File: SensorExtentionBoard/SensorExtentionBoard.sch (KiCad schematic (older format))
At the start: 0 parts

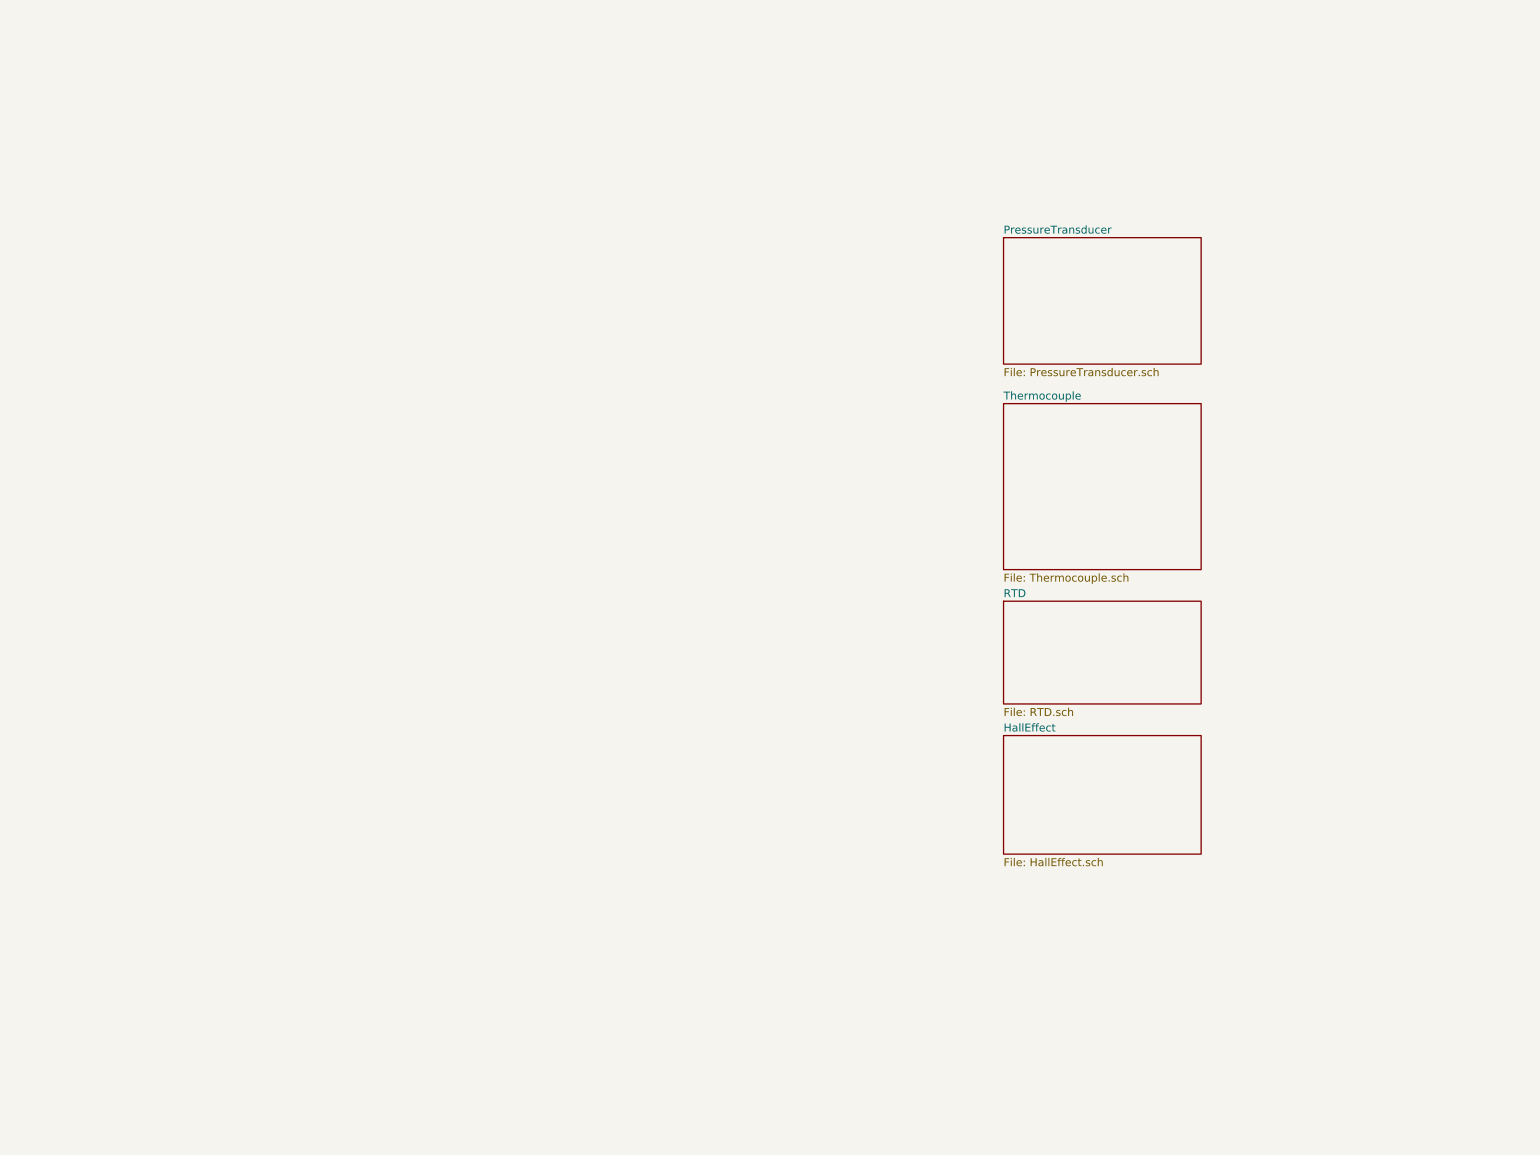
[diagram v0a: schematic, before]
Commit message: Added top level page and made various fixes in other pages of SEB test rig board
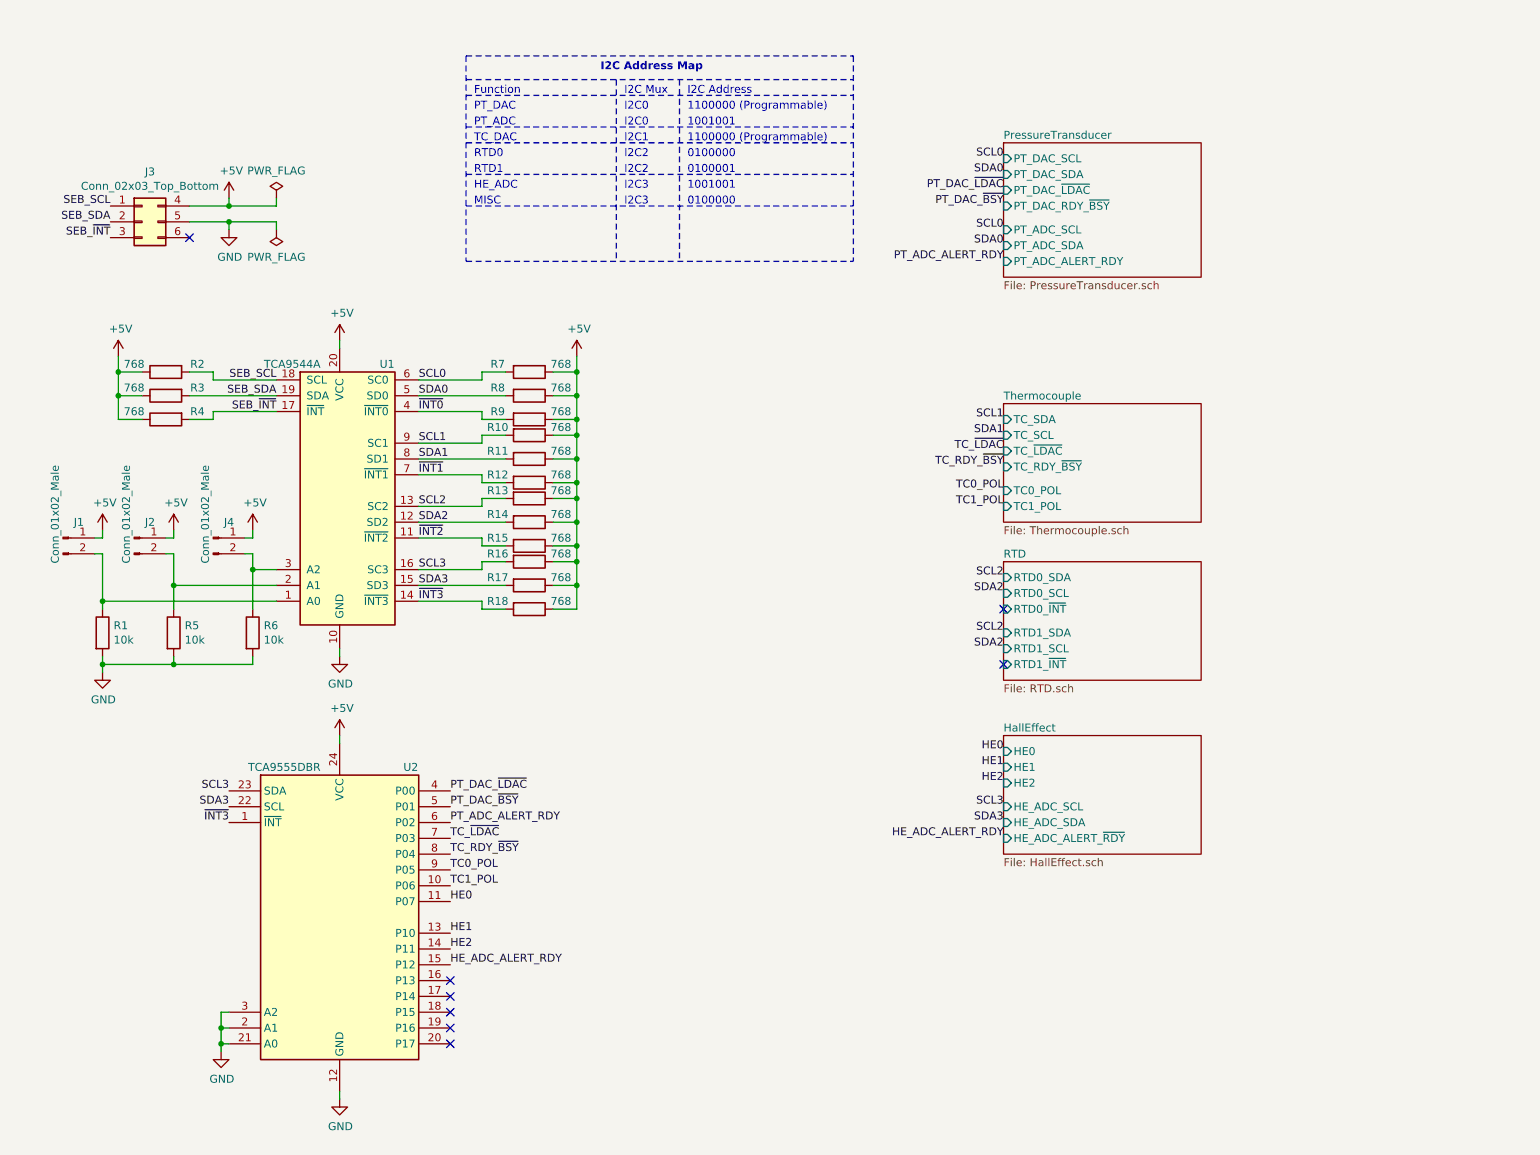
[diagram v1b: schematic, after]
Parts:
- added J1, J2, J4: Conn_01x02_Male, symbol Connector:Conn_01x02_Male
- added J3: Conn_02x03_Top_Bottom, symbol Connector_Generic:Conn_02x03_Top_Bottom
- added R1, R5, R6: 10k, Resistor_SMD:R_1206_3216Metric_Pad1.42x1.75mm_HandSolder, symbol Device:R
- added R10, R11, R12, R13, R14, R15, R16, R17, R18, R2, R3, R4, R7, R8, R9: 768, Resistor_SMD:R_1206_3216Metric_Pad1.42x1.75mm_HandSolder, symbol Device:R
- added U1: TCA9544A, Package_SO:TSSOP-20_4.4x6.5mm_P0.65mm, symbol Interface_Expansion:TCA9544A
- added U2: TCA9555DBR, Package_SO:SSOP-24_5.3x8.2mm_P0.65mm, symbol Interface_Expansion:TCA9555DBR
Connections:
- new net: J4.2 (Pin_2), R6.1, U1.3 (A2)
- new net: J2.2 (Pin_2), R5.1, U1.2 (A1)
- new net: J1.2 (Pin_2), R1.1, U1.1 (A0)
- new net +5V: J1.1 (Pin_1), J2.1 (Pin_1), J3.4 (Pin_4), J4.1 (Pin_1), R10.1, R11.1, R12.1, R13.1, R14.1, R15.1, R16.1, R17.1, R18.1, R2.1, R3.1, R4.1, R7.1, R8.1, R9.1, U1.20 (VCC), U2.24 (VCC)
- new net GND: J3.5 (Pin_5), R1.2, R5.2, R6.2, U1.10 (GND), U2.12 (GND), U2.2 (A1), U2.21 (A0), U2.3 (A2)
- new net HE0: U2.11 (P07)
- new net HE1: U2.13 (P10)
- new net HE2: U2.14 (P11)
- new net HE_ADC_ALERT_RDY: U2.15 (P12)
- new net PT_ADC_ALERT_RDY: U2.6 (P02)
- new net PT_DAC_~BSY: U2.5 (P01)
- new net PT_DAC_~LDAC: U2.4 (P00)
- new net SCL0: R7.2, U1.6 (SC0)
- new net SCL1: R10.2, U1.9 (SC1)
- new net SCL2: R13.2, U1.13 (SC2)
- new net SCL3: R16.2, U1.16 (SC3), U2.23 (SDA)
- new net SDA0: R8.2, U1.5 (SD0)
- new net SDA1: R11.2, U1.8 (SD1)
- new net SDA2: R14.2, U1.12 (SD2)
- new net SDA3: R17.2, U1.15 (SD3), U2.22 (SCL)
- new net SEB_SCL: J3.1 (Pin_1), R2.2, U1.18 (SCL)
- new net SEB_SDA: J3.2 (Pin_2), R3.2, U1.19 (SDA)
- new net SEB_~INT: J3.3 (Pin_3), R4.2, U1.17 (~INT)
- new net TC0_POL: U2.9 (P05)
- new net TC1_POL: U2.10 (P06)
- new net TC_RDY_~BSY: U2.8 (P04)
- new net TC_~LDAC: U2.7 (P03)
- new net ~INT0: R9.2, U1.4 (~INT0)
- new net ~INT1: R12.2, U1.7 (~INT1)
- new net ~INT2: R15.2, U1.11 (~INT2)
- new net ~INT3: R18.2, U1.14 (~INT3), U2.1 (~INT)
- no-connect marks 0 -> 8
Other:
- note added: "0100000"
- note added: "0100001"
- note added: "1001001"
- note added: "1100000 (Programmable)"
- note added: "Function"
- note added: "HE_ADC"
- note added: "I2C Address"
- note added: "I2C Address Map"
- note added: "I2C Mux"
- note added: "I2C0"
- note added: "I2C1"
- note added: "I2C2"
- note added: "I2C3"
- note added: "MISC"
- note added: "PT_ADC"
- note added: "PT_DAC"
- note added: "RTD0"
- note added: "RTD1"
- note added: "TC_DAC"

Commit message: Moved some stuff and added footprints to components
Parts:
- J1, J2, J4: footprint (none) -> Connector_PinHeader_2.54mm:PinHeader_1x02_P2.54mm_Vertical
- J3: footprint (none) -> Connector_Molex:Molex_Micro-Fit_3.0_43045-0612_2x03_P3.00mm_Vertical
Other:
- note added: "I2C Address 1110xxx"
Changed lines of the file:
@@
 $EndDescr
 $Sheet
-S 6750 5050 1250 750
+S 8750 5100 1250 750
 U 5E059E7A
 F0 "HallEffect" 50
 F1 "HallEffect.sch" 50
-F2 "HE0" I L 6750 5150 50
-F3 "HE1" I L 6750 5250 50
-F4 "HE2" I L 6750 5350 50
-F5 "HE_ADC_ALERT_~RDY" I L 6750 5700 50
-F6 "HE_ADC_SCL" I L 6750 5500 50
-F7 "HE_ADC_SDA" I L 6750 5600 50
+F2 "HE0" I L 8750 5200 50
+F3 "HE1" I L 8750 5300 50
+F4 "HE2" I L 8750 5400 50
+F5 "HE_ADC_ALERT_~RDY" I L 8750 5750 50
+F6 "HE_ADC_SCL" I L 8750 5550 50
+F7 "HE_ADC_SDA" I L 8750 5650 50
 $EndSheet
 $Sheet
-S 6750 2950 1250 750
+S 8750 3000 1250 750
 U 5E059E8F
 F0 "Thermocouple" 50
 F1 "Thermocouple.sch" 50
-F2 "TC_SDA" I L 6750 3050 50
-F3 "TC_SCL" I L 6750 3150 50
-F4 "TC_~LDAC" I L 6750 3250 50
-F5 "TC_RDY_~BSY" I L 6750 3350 50
-F6 "TC0_POL" I L 6750 3500 50
-F7 "TC1_POL" I L 6750 3600 50
+F2 "TC_SDA" I L 8750 3100 50
+F3 "TC_SCL" I L 8750 3200 50
+F4 "TC_~LDAC" I L 8750 3300 50
+F5 "TC_RDY_~BSY" I L 8750 3400 50
+F6 "TC0_POL" I L 8750 3550 50
+F7 "TC1_POL" I L 8750 3650 50
 $EndSheet
 $Sheet
-S 6750 3950 1250 750
+S 8750 4000 1250 750
 U 5E059E9F
 F0 "RTD" 50
 F1 "RTD.sch" 50
-F2 "RTD0_SDA" I L 6750 4050 50
-F3 "RTD0_SCL" I L 6750 4150 50
-F4 "RTD0_~INT" I L 6750 4250 50
-F5 "RTD1_SDA" I L 6750 4400 50
-F6 "RTD1_SCL" I L 6750 4500 50
-F7 "RTD1_~INT" I L 6750 4600 50
+F2 "RTD0_SDA" I L 8750 4100 50
+F3 "RTD0_SCL" I L 8750 4200 50
+F4 "RTD0_~INT" I L 8750 4300 50
+F5 "RTD1_SDA" I L 8750 4450 50
+F6 "RTD1_SCL" I L 8750 4550 50
+F7 "RTD1_~INT" I L 8750 4650 50
 $EndSheet
 Text Label 2150 2800 2    50   ~ 0
@@
 F 0 "J3" H 1350 2117 50  0000 C CNN
 F 1 "Conn_02x03_Top_Bottom" H 1350 2026 50  0000 C CNN
-F 2 "" H 1300 1800 50  0001 C CNN
+F 2 "Connector_Molex:Molex_Micro-Fit_3.0_43045-0612_2x03_P3.00mm_Vertical" H 1300 1800 50  0001 C CNN
 F 3 "~" H 1300 1800 50  0001 C CNN
 	1    1300 1800
@@
 Connection ~ 1850 1700
 NoConn ~ 1600 1900
-Text Notes 3400 1000 0    50   ~ 0
+Text Notes 4800 1000 0    50   ~ 0
 Function
-Text Notes 4350 1000 0    50   ~ 0
+Text Notes 5750 1000 0    50   ~ 0
 I2C Mux
-Text Notes 4750 1000 0    50   ~ 0
+Text Notes 6150 1000 0    50   ~ 0
 I2C Address
 Wire Notes Line style solid
-	4300 900  4300 2050
+	5700 900  5700 2050
 Wire Notes Line style solid
-	4700 900  4700 2050
-Text Notes 4200 850  0    50   ~ 10
+	6100 900  6100 2050
+Text Notes 5600 850  0    50   ~ 10
 I2C Address Map
 Wire Notes Line style solid
-	3350 750  3350 2050
+	4750 750  4750 2050
 Wire Notes Line style solid
-	5800 750  5800 2050
-Text Notes 4750 1100 0    50   ~ 0
+	7200 750  7200 2050
+Text Notes 6150 1100 0    50   ~ 0
 1100000 (Programmable)
-Text Notes 3400 1100 0    50   ~ 0
+Text Notes 4800 1100 0    50   ~ 0
 PT_DAC
-Text Notes 4350 1100 0    50   ~ 0
+Text Notes 5750 1100 0    50   ~ 0
 I2C0
 Wire Notes Line style solid
-	3350 900  5800 900
+	4750 900  7200 900
 Wire Notes Line style solid
-	3350 750  5800 750
+	4750 750  7200 750
 Wire Notes Line style solid
-	3350 2050 5800 2050
-Text Notes 3400 1200 0    50   ~ 0
+	4750 2050 7200 2050
+Text Notes 4800 1200 0    50   ~ 0
 PT_ADC
-Text Notes 4750 1200 0    50   ~ 0
+Text Notes 6150 1200 0    50   ~ 0
 1001001
-Text Notes 4350 1200 0    50   ~ 0
+Text Notes 5750 1200 0    50   ~ 0
 I2C0
-Text Notes 4750 1300 0    50   ~ 0
+Text Notes 6150 1300 0    50   ~ 0
 1100000 (Programmable)
-Text Notes 4350 1300 0    50   ~ 0
+Text Notes 5750 1300 0    50   ~ 0
 I2C1
-Text Notes 3400 1300 0    50   ~ 0
+Text Notes 4800 1300 0    50   ~ 0
 TC_DAC
-Text Notes 3400 1400 0    50   ~ 0
+Text Notes 4800 1400 0    50   ~ 0
 RTD0
-Text Notes 3400 1500 0    50   ~ 0
+Text Notes 4800 1500 0    50   ~ 0
 RTD1
-Text Notes 4750 1400 0    50   ~ 0
+Text Notes 6150 1400 0    50   ~ 0
 0100000
-Text Notes 4750 1500 0    50   ~ 0
+Text Notes 6150 1500 0    50   ~ 0
 0100001
-Text Notes 4350 1400 0    50   ~ 0
+Text Notes 5750 1400 0    50   ~ 0
 I2C2
-Text Notes 4350 1500 0    50   ~ 0
+Text Notes 5750 1500 0    50   ~ 0
 I2C2
 Wire Notes Line style solid
-	3350 1000 5800 1000
+	4750 1000 7200 1000
 $Comp
 L power:GND #PWR02
@@
 F 0 "J4" H 1850 3900 50  0000 C CNN
 F 1 "Conn_01x02_Male" V 1700 3950 50  0000 C CNN
-F 2 "" H 1750 3800 50  0001 C CNN
+F 2 "Connector_PinHeader_2.54mm:PinHeader_1x02_P2.54mm_Vertical" H 1750 3800 50  0001 C CNN
 F 3 "~" H 1750 3800 50  0001 C CNN
 	1    1750 3800
@@
 F 0 "J2" H 1350 3900 50  0000 C CNN
 F 1 "Conn_01x02_Male" V 1200 3950 50  0000 C CNN
-F 2 "" H 1250 3800 50  0001 C CNN
+F 2 "Connector_PinHeader_2.54mm:PinHeader_1x02_P2.54mm_Vertical" H 1250 3800 50  0001 C CNN
 F 3 "~" H 1250 3800 50  0001 C CNN
 	1    1250 3800
@@
 F 0 "J1" H 900 3900 50  0000 C CNN
 F 1 "Conn_01x02_Male" V 750 3950 50  0000 C CNN
-F 2 "" H 800 3800 50  0001 C CNN
+F 2 "Connector_PinHeader_2.54mm:PinHeader_1x02_P2.54mm_Vertical" H 800 3800 50  0001 C CNN
 F 3 "~" H 800 3800 50  0001 C CNN
 	1    800  3800
@@
 Text Label 1100 1900 2    50   ~ 0
 SEB_~INT
-Text Notes 3400 1600 0    50   ~ 0
+Text Notes 4800 1600 0    50   ~ 0
 HE_ADC
-Text Notes 4350 1600 0    50   ~ 0
+Text Notes 5750 1600 0    50   ~ 0
 I2C3
-Text Notes 4750 1600 0    50   ~ 0
+Text Notes 6150 1600 0    50   ~ 0
 1001001
 Text Label 3050 2800 0    50   ~ 0
@@
 Text Label 3050 4200 0    50   ~ 0
 ~INT3
-Text Label 6750 1400 2    50   ~ 0
+Text Label 8750 2000 2    50   ~ 0
 SCL0
-Text Label 6750 1500 2    50   ~ 0
+Text Label 8750 2100 2    50   ~ 0
 SDA0
-Text Label 6750 1850 2    50   ~ 0
+Text Label 8750 2450 2    50   ~ 0
 SCL0
-Text Label 6750 1950 2    50   ~ 0
+Text Label 8750 2550 2    50   ~ 0
 SDA0
-Text Label 6750 3050 2    50   ~ 0
+Text Label 8750 3100 2    50   ~ 0
 SCL1
-Text Label 6750 3150 2    50   ~ 0
+Text Label 8750 3200 2    50   ~ 0
 SDA1
-Text Label 6750 4050 2    50   ~ 0
+Text Label 8750 4100 2    50   ~ 0
 SCL2
-Text Label 6750 4150 2    50   ~ 0
+Text Label 8750 4200 2    50   ~ 0
 SDA2
-Text Label 6750 4400 2    50   ~ 0
+Text Label 8750 4450 2    50   ~ 0
 SCL2
-Text Label 6750 4500 2    50   ~ 0
+Text Label 8750 4550 2    50   ~ 0
 SDA2
-Text Label 6750 5500 2    50   ~ 0
+Text Label 8750 5550 2    50   ~ 0
 SCL3
-Text Label 6750 5600 2    50   ~ 0
+Text Label 8750 5650 2    50   ~ 0
 SDA3
 $Comp
@@
 Wire Wire Line
 	2550 5050 2550 5100
-Text Notes 3400 1700 0    50   ~ 0
+Text Notes 4800 1700 0    50   ~ 0
 MISC
-Text Notes 4350 1700 0    50   ~ 0
+Text Notes 5750 1700 0    50   ~ 0
 I2C3
-Text Notes 4750 1700 0    50   ~ 0
+Text Notes 6150 1700 0    50   ~ 0
 0100000
 Wire Notes Line
-	3350 1200 5800 1200
+	4750 1200 7200 1200
 Wire Notes Line
-	3350 1300 5800 1300
+	4750 1300 7200 1300
 Wire Notes Line
-	3350 1500 5800 1500
+	4750 1500 7200 1500
 Wire Notes Line
-	3350 1700 5800 1700
+	4750 1700 7200 1700
 $Sheet
-S 6750 1300 1250 850
+S 8750 1900 1250 850
 U 5E059EAC
 F0 "PressureTransducer" 50
 F1 "PressureTransducer.sch" 50
-F2 "PT_DAC_SCL" I L 6750 1400 50
-F3 "PT_DAC_SDA" I L 6750 1500 50
-F4 "PT_DAC_RDY_~BSY" I L 6750 1700 50
-F5 "PT_ADC_SCL" I L 6750 1850 50
-F6 "PT_ADC_SDA" I L 6750 1950 50
-F7 "PT_ADC_ALERT_RDY" I L 6750 2050 50
-F8 "PT_DAC_~LDAC" I L 6750 1600 50
+F2 "PT_DAC_SCL" I L 8750 2000 50
+F3 "PT_DAC_SDA" I L 8750 2100 50
+F4 "PT_DAC_RDY_~BSY" I L 8750 2300 50
+F5 "PT_ADC_SCL" I L 8750 2450 50
+F6 "PT_ADC_SDA" I L 8750 2550 50
+F7 "PT_ADC_ALERT_RDY" I L 8750 2650 50
+F8 "PT_DAC_~LDAC" I L 8750 2200 50
 $EndSheet
 Text Label 3250 6100 0    50   ~ 0
@@
 Text Label 3250 6400 0    50   ~ 0
 HE2
-Text Label 6750 5350 2    50   ~ 0
+Text Label 8750 5400 2    50   ~ 0
 HE2
-Text Label 6750 5250 2    50   ~ 0
+Text Label 8750 5300 2    50   ~ 0
 HE1
-Text Label 6750 5150 2    50   ~ 0
+Text Label 8750 5200 2    50   ~ 0
 HE0
-Text Label 6750 3500 2    50   ~ 0
+Text Label 8750 3550 2    50   ~ 0
 TC0_POL
-Text Label 6750 3600 2    50   ~ 0
+Text Label 8750 3650 2    50   ~ 0
 TC1_POL
 Text Label 3250 5900 0    50   ~ 0
@@
 Text Label 3250 6000 0    50   ~ 0
 TC1_POL
-Text Label 6750 3250 2    50   ~ 0
+Text Label 8750 3300 2    50   ~ 0
 TC_~LDAC
-Text Label 6750 3350 2    50   ~ 0
+Text Label 8750 3400 2    50   ~ 0
 TC_RDY_~BSY
 Text Label 3250 5700 0    50   ~ 0
@@
 Text Label 3250 5800 0    50   ~ 0
 TC_RDY_~BSY
-Text Label 6750 1600 2    50   ~ 0
+Text Label 8750 2200 2    50   ~ 0
 PT_DAC_~LDAC
-Text Label 6750 1700 2    50   ~ 0
+Text Label 8750 2300 2    50   ~ 0
 PT_DAC_~BSY
-Text Label 6750 2050 2    50   ~ 0
+Text Label 8750 2650 2    50   ~ 0
 PT_ADC_ALERT_RDY
 Text Label 3250 5400 0    50   ~ 0
@@
 Text Label 3250 5600 0    50   ~ 0
 PT_ADC_ALERT_RDY
-Text Label 6750 5700 2    50   ~ 0
+Text Label 8750 5750 2    50   ~ 0
 HE_ADC_ALERT_RDY
 Text Label 3250 6500 0    50   ~ 0
@@
 	1    0    0    -1
 $EndComp
-NoConn ~ 6750 4250
-NoConn ~ 6750 4600
+NoConn ~ 8750 4300
+NoConn ~ 8750 4650
 NoConn ~ 3250 6600
 NoConn ~ 3250 6700
@@
 	1    0    0    -1
 $EndComp
+Text Notes 2650 2550 0    50   ~ 0
+I2C Address 1110xxx
 $EndSCHEMATC
